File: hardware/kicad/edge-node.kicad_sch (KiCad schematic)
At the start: 0 parts

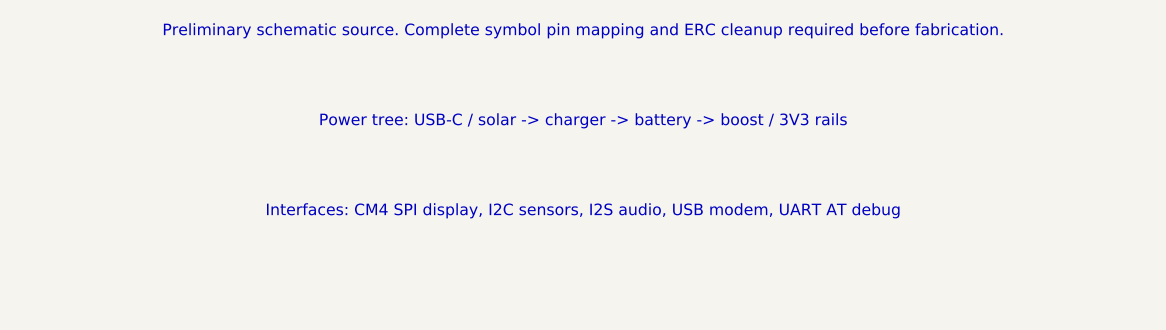
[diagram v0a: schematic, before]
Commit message: Add smartphone-first prototype and hosted backend
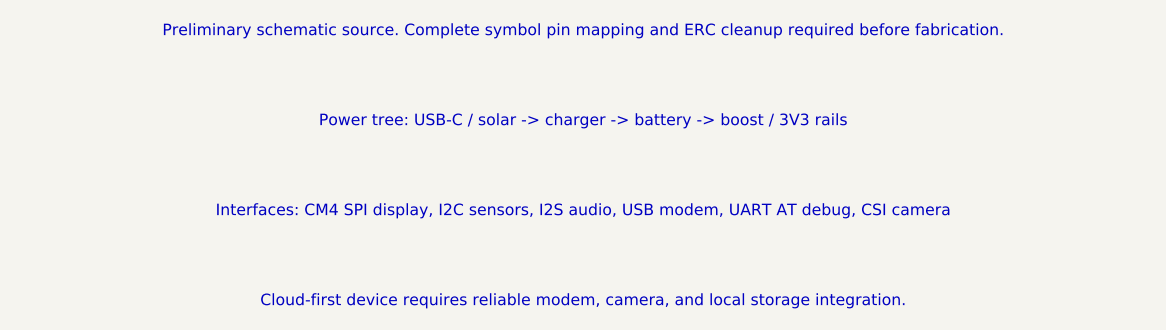
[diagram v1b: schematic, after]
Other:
- note added: "Cloud-first device requires reliable modem, camera, and local storage integration."
- note added: "Interfaces: CM4 SPI display, I2C sensors, I2S audio, USB modem, UART AT debug, CSI camera"
- note removed: "Interfaces: CM4 SPI display, I2C sensors, I2S audio, USB modem, UART AT debug"
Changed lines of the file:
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@@
   (text "Preliminary schematic source. Complete symbol pin mapping and ERC cleanup required before fabrication." (at 35 20 0))
   (text "Power tree: USB-C / solar -> charger -> battery -> boost / 3V3 rails" (at 35 30 0))
-  (text "Interfaces: CM4 SPI display, I2C sensors, I2S audio, USB modem, UART AT debug" (at 35 40 0))
+  (text "Interfaces: CM4 SPI display, I2C sensors, I2S audio, USB modem, UART AT debug, CSI camera" (at 35 40 0))
+  (text "Cloud-first device requires reliable modem, camera, and local storage integration." (at 35 50 0))
 )
